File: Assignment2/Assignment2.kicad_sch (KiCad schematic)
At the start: 37 parts, among them J1 USB_B_Micro, J2 Conn_01x02, J3 Conn_01x03, J4 Conn_01x02, SW1 SW_Push, U1 RP2040, U2 NCP1117-3.3_SOT223, U3 W25Q128JVS, U4 ABM8-272-T3, U5 MAX98357A

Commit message: assignment2: microphone and color module
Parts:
- added C19: 0.1μF, Capacitor_SMD:C_0603_1608Metric, symbol Device:C
- added C20: 200pF, Capacitor_SMD:C_0603_1608Metric, symbol Device:C
- added C21: 100nF, Capacitor_SMD:C_0603_1608Metric, symbol Device:C
- added MK1: SPH0645LM4H, Sensor_Audio:Knowles_SPH0645LM4H-6_3.5x2.65mm, symbol Sensor_Audio:SPH0645LM4H
- added R10, R9: 2.2kΩ, Resistor_SMD:R_0603_1608Metric, symbol Device:R
- added R6, R7, R8: 51Ω, Resistor_SMD:R_0603_1608Metric, symbol Device:R
- added U6: VEML6040, VEML6040:VISHAY_VEML6040_1.25X2X1, symbol VEML6040:VEML6040
- C1, C17, C2: value 10u -> 10μF
- C10, C11, C12, C13, C14, C15, C16, C7, C8: value 100n -> 100nF
- C18: value 0.1u -> 0.1μF
- C3: value 100u -> 100μF
- C4, C5: value 15p -> 15pF
- C6, C9: value 1u -> 1μF
- R1: value 1k -> 1kΩ
- R3, R4: value 27 -> 27Ω
- R5: value 1M -> 1MΩ
- U3: footprint Package_SO:SOIC-8_5.23x5.23mm_P1.27mm -> Package_SO:SOIC-8_5.3x5.3mm_P1.27mm
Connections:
- net +3.3V: now also C19.2, C20.2, C21.2, MK1.5 (VDD), R10.2, R9.2, U6.4
- net GND: now also C19.1, C20.1, C21.1, MK1.2 (SEL), MK1.3 (GND), U6.1
- net GPIO3: now reaches U1.5 (GPIO3)
- net GPIO3: now also R8.2
- net GPIO4: now reaches U1.6 (GPIO4)
- net GPIO4: now also R7.1
- net GPIO5: now reaches U1.7 (GPIO5)
- net GPIO5: now also R6.1
- net GPIO6: now reaches U1.8 (GPIO6)
- net GPIO6: now also R9.1, U6.2
- net GPIO7: now reaches U1.9 (GPIO7)
- net GPIO7: now also R10.1, U6.3
- new net: MK1.1 (WS), R6.2
- new net: MK1.4 (BCLK), R7.2
- new net: MK1.6 (DATA), R8.1
- no-connect marks 29 -> 23
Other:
- note added: "C6 must be close to VREG_VOUT"
- note added: "C9 must be close to VREG_VIN"
- note added: "Decoupling (C19) and RF Filter (C20) capacitor should be closest to the microphone and use short, wide trace to minimize inductance."
- note added: "Microphone Unit"
- note added: "Power and Data Unit"
- note added: "Todo List 1. Add Input Audio Unit - DONE 2. Add Color Sensor Unit - DONE 3. Fill in the Footprint - SW Footprint OK? 4. Route and place"
- note added: "Use VIA to connect microphone's ground pad to other layer's ground pane."
- note removed: "Power Unit"
- note removed: "Todo List 1. Add Input Audio Unit 2. Add Color Sensor Unit 3. Fill in the Footprint 4. Route and place"
- moved on the sheet: C11, C12, C13, C14, C15, C16, C17, C18, J4, R5, U5

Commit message: assignment2: add leds
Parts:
- added D1, D2: LED, LED_SMD:LED_0603_1608Metric, symbol Device:LED
- added R11, R12: 150Ω, Resistor_SMD:R_0603_1608Metric, symbol Device:R
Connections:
- net GND: now also D1.1 (K), D2.1 (K)
- net GPIO8: now reaches U1.11 (GPIO8)
- net GPIO8: now also R11.1
- net GPIO9: now reaches U1.12 (GPIO9)
- net GPIO9: now also R12.1
- new net: D2.2 (A), R12.2
- new net: D1.2 (A), R11.2
- no-connect marks 23 -> 21
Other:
- note added: "LED Module"

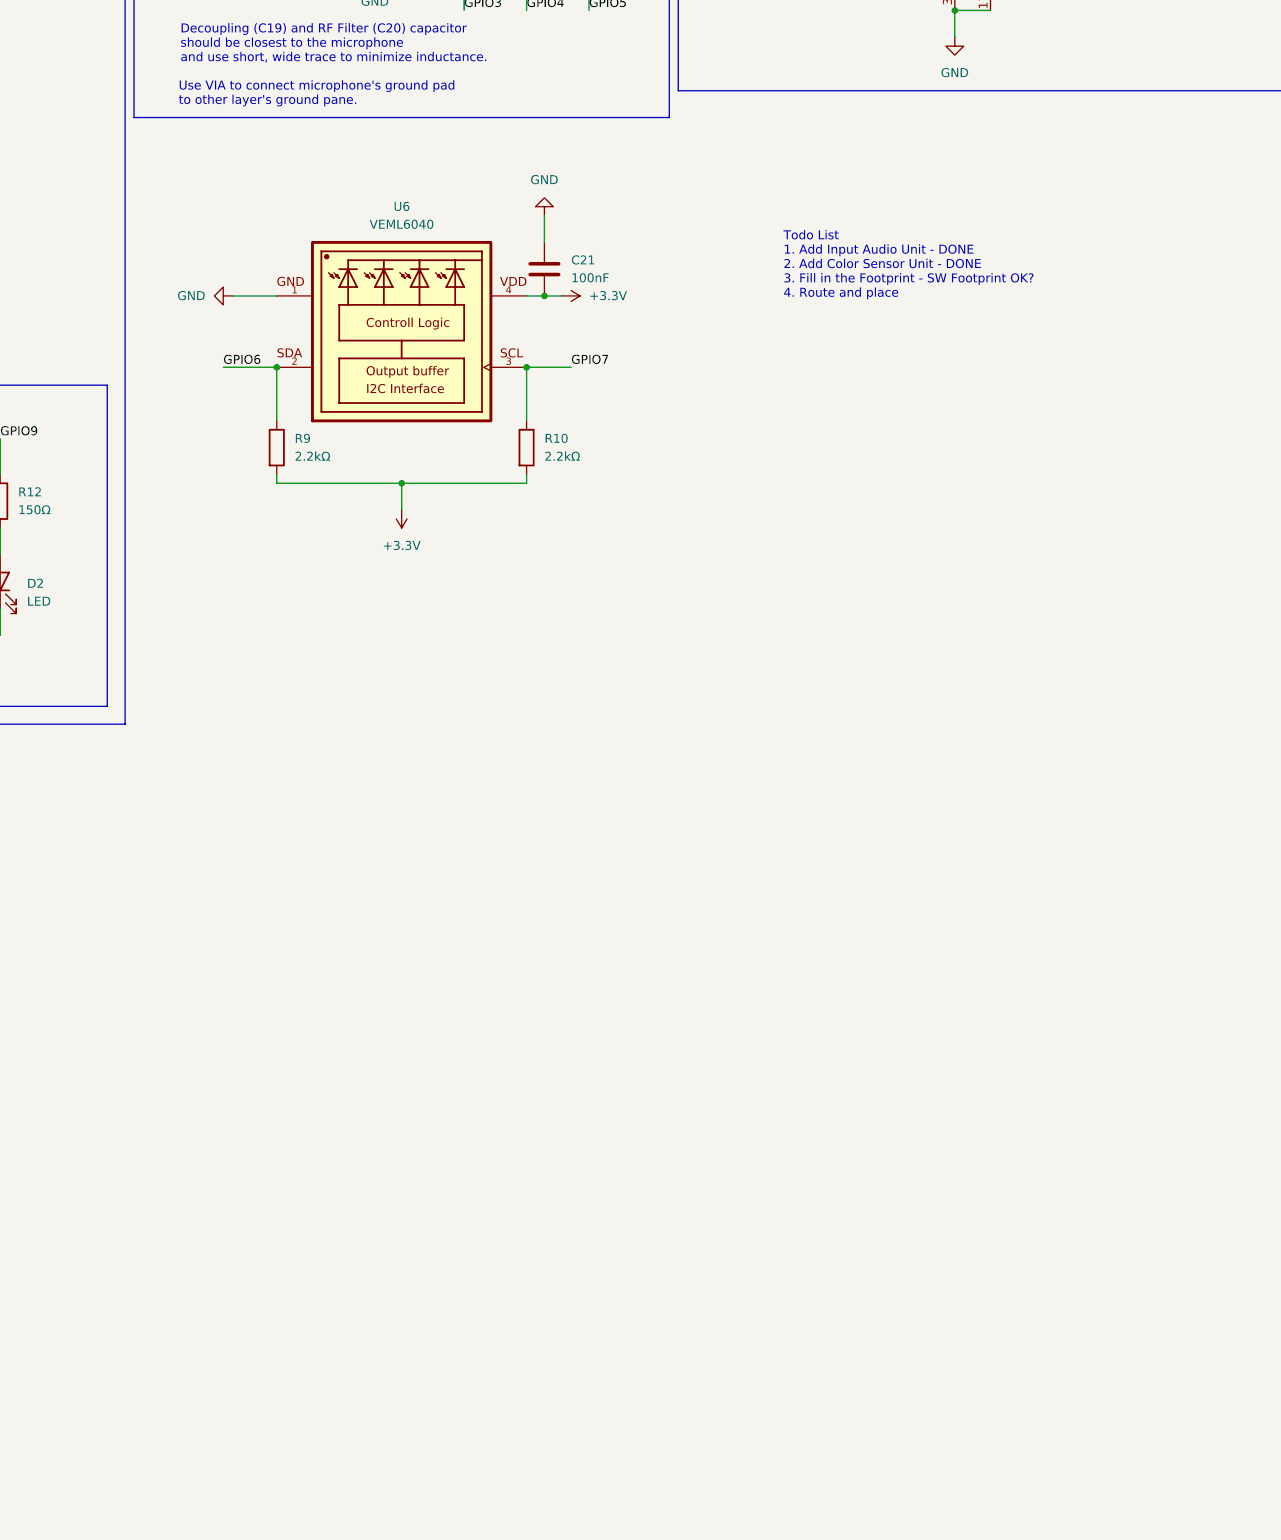
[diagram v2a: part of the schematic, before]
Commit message: assignment2: complete schematic
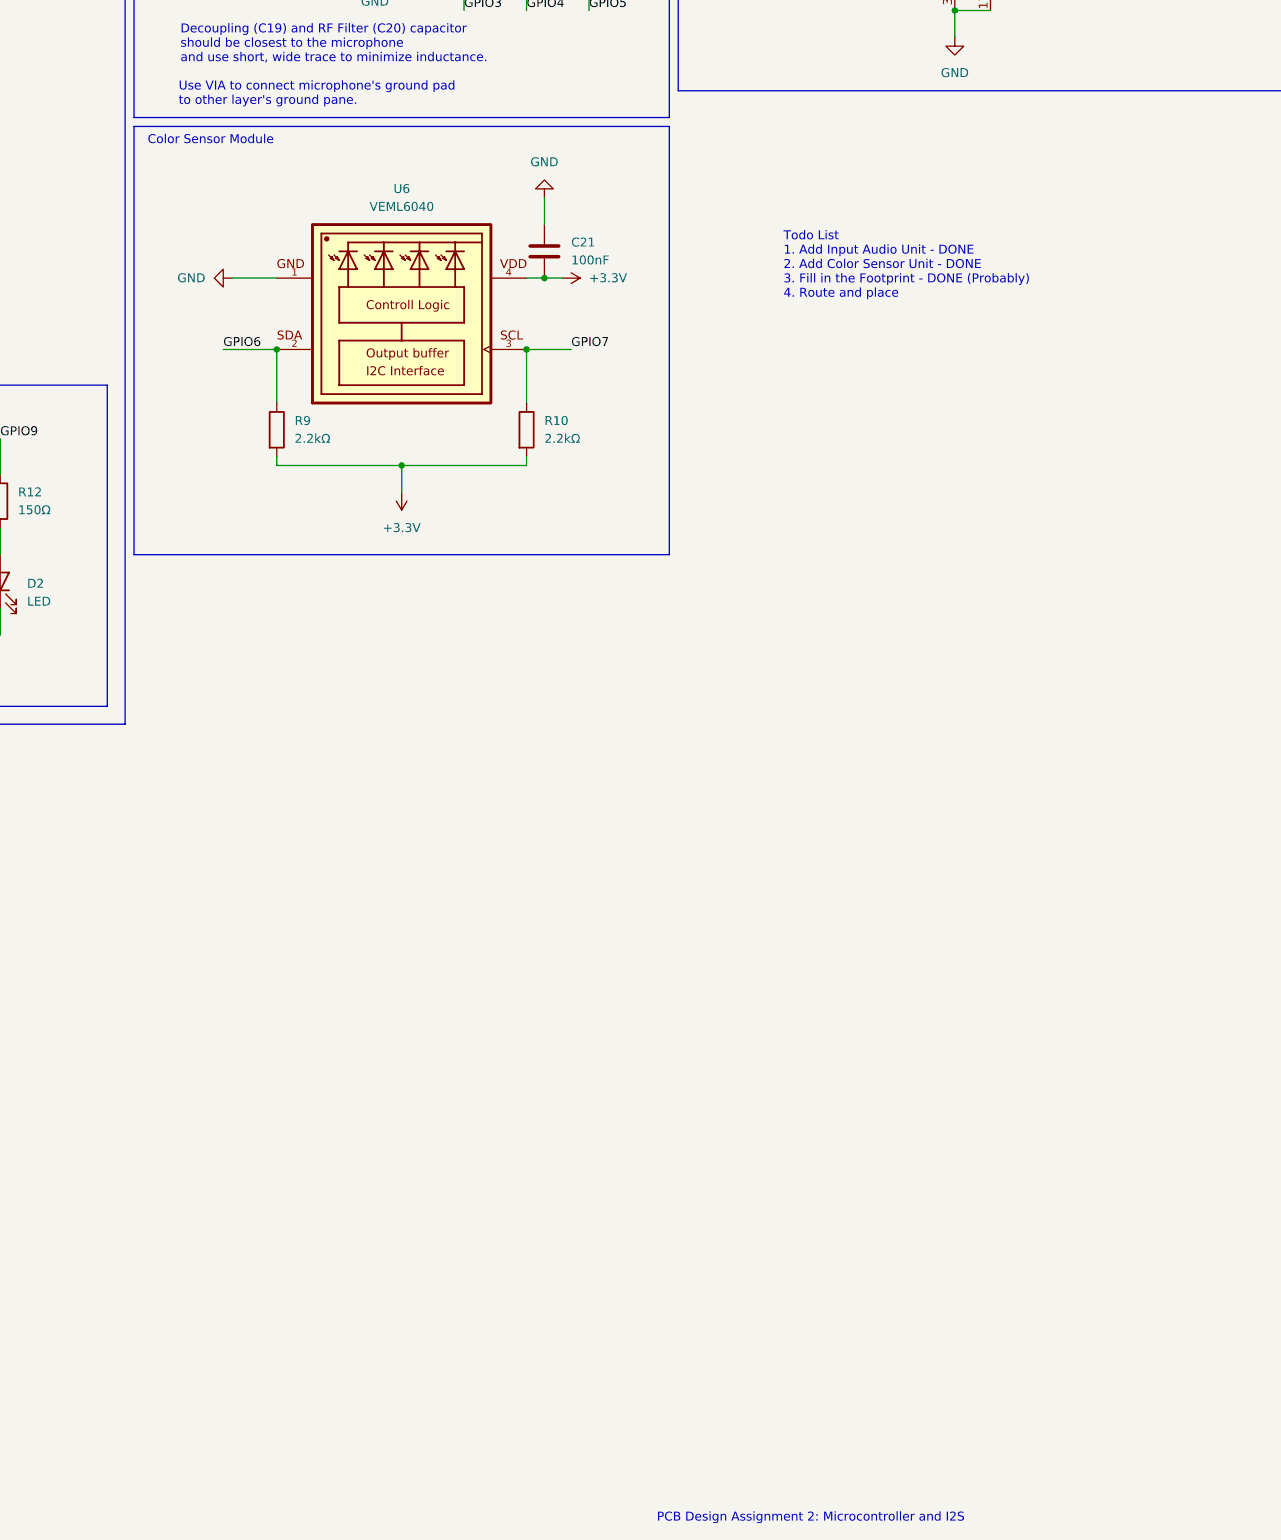
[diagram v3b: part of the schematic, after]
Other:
- note added: "Color Sensor Module"
- note added: "PCB Design Assignment 2: Microcontroller and I2S"
- note added: "Todo List 1. Add Input Audio Unit - DONE 2. Add Color Sensor Unit - DONE 3. Fill in the Footprint - DONE (Probably) 4. Route and place"
- note removed: "Todo List 1. Add Input Audio Unit - DONE 2. Add Color Sensor Unit - DONE 3. Fill in the Footprint - SW Footprint OK? 4. Route and place"
- moved on the sheet: C21, R10, R9, U6

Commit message: swap c19 and c20, add silkscreen and round corner
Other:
- note added: "Decoupling (C19) and RF Filter (C20) capacitor should be close to the microphone (RF Filter be closest) and use short, wide trace to minimize inductance."
- note removed: "Decoupling (C19) and RF Filter (C20) capacitor should be closest to the microphone and use short, wide trace to minimize inductance."
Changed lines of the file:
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@@
 		)
 	)
-	(text "Decoupling (C19) and RF Filter (C20) capacitor\nshould be closest to the microphone\nand use short, wide trace to minimize inductance."
+	(text "Decoupling (C19) and RF Filter (C20) capacitor\nshould be close to the microphone (RF Filter be closest)\nand use short, wide trace to minimize inductance."
 		(exclude_from_sim no)
 		(at 241.554 67.056 0)
